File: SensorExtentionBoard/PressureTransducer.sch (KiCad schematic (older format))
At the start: 10 parts

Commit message: Added Hall Effect sensor test circuit
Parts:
- removed R? (x3): 768, symbol Device:R
- removed R? (x3): 12, symbol Device:R
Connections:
- wire segments 39 -> 18
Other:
- note removed: "Each pair of resistors in voltage divider must have a similar temperature coefficient (like from the same resistor family)"
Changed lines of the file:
@@
 	4900 3350 4900 3300
 NoConn ~ 5500 3100
-$Comp
-L Device:R R?
-U 1 1 5E062611
-P 5700 3300
-F 0 "R?" H 5770 3346 50  0000 L CNN
-F 1 "768" H 5770 3255 50  0000 L CNN
-F 2 "" V 5630 3300 50  0001 C CNN
-F 3 "~" H 5700 3300 50  0001 C CNN
-	1    5700 3300
-	1    0    0    -1
-$EndComp
-$Comp
-L Device:R R?
-U 1 1 5E062617
-P 5700 3900
-F 0 "R?" H 5770 3946 50  0000 L CNN
-F 1 "12" H 5770 3855 50  0000 L CNN
-F 2 "" V 5630 3900 50  0001 C CNN
-F 3 "~" H 5700 3900 50  0001 C CNN
-	1    5700 3900
-	1    0    0    -1
-$EndComp
-Wire Wire Line
-	6300 3450 6300 3500
-Wire Wire Line
-	6000 3450 6000 3600
-Wire Wire Line
-	5700 3450 5700 3700
-Wire Wire Line
-	6300 3500 6750 3500
-Connection ~ 6300 3500
-Wire Wire Line
-	6300 3500 6300 3750
-Wire Wire Line
-	6000 3600 6750 3600
-Connection ~ 6000 3600
-Wire Wire Line
-	6000 3600 6000 3750
-Wire Wire Line
-	5700 3700 6750 3700
-Connection ~ 5700 3700
-Wire Wire Line
-	5700 3700 5700 3750
-Wire Wire Line
-	5500 3000 5700 3000
-Wire Wire Line
-	5700 3000 5700 3150
-Wire Wire Line
-	5500 2900 6000 2900
-Wire Wire Line
-	6000 2900 6000 3150
-Wire Wire Line
-	5500 2800 6300 2800
-Wire Wire Line
-	6300 2800 6300 3150
-$Comp
-L power:GND #PWR?
-U 1 1 5E068856
-P 5700 4150
-F 0 "#PWR?" H 5700 3900 50  0001 C CNN
-F 1 "GND" H 5705 3977 50  0000 C CNN
-F 2 "" H 5700 4150 50  0001 C CNN
-F 3 "" H 5700 4150 50  0001 C CNN
-	1    5700 4150
-	1    0    0    -1
-$EndComp
-Wire Wire Line
-	5700 4050 5700 4100
-Wire Wire Line
-	5700 4100 6000 4100
-Wire Wire Line
-	6000 4100 6000 4050
-Connection ~ 5700 4100
-Wire Wire Line
-	5700 4100 5700 4150
-Wire Wire Line
-	6000 4100 6300 4100
-Wire Wire Line
-	6300 4100 6300 4050
-Connection ~ 6000 4100
-Text Label 6750 3500 0    50   ~ 0
+Text Label 5500 2800 0    50   ~ 0
 PT0
-Text Label 6750 3600 0    50   ~ 0
+Text Label 5500 2900 0    50   ~ 0
 PT1
-Text Label 6750 3700 0    50   ~ 0
+Text Label 5500 3000 0    50   ~ 0
 PT2
 Wire Wire Line
@@
 Wire Wire Line
 	4300 3100 4250 3100
-Text Notes 5700 2300 0    50   ~ 0
-Each pair of resistors in voltage divider must have a similar temperature coefficient (like from the same resistor family)
-$Comp
-L Device:R R?
-U 1 1 5EAFB0C7
-P 6000 3300
-F 0 "R?" H 6070 3346 50  0000 L CNN
-F 1 "768" H 6070 3255 50  0000 L CNN
-F 2 "" V 5930 3300 50  0001 C CNN
-F 3 "~" H 6000 3300 50  0001 C CNN
-	1    6000 3300
-	1    0    0    -1
-$EndComp
-$Comp
-L Device:R R?
-U 1 1 5EAFB244
-P 6300 3300
-F 0 "R?" H 6370 3346 50  0000 L CNN
-F 1 "768" H 6370 3255 50  0000 L CNN
-F 2 "" V 6230 3300 50  0001 C CNN
-F 3 "~" H 6300 3300 50  0001 C CNN
-	1    6300 3300
-	1    0    0    -1
-$EndComp
-$Comp
-L Device:R R?
-U 1 1 5EAFB46A
-P 6000 3900
-F 0 "R?" H 6070 3946 50  0000 L CNN
-F 1 "12" H 6070 3855 50  0000 L CNN
-F 2 "" V 5930 3900 50  0001 C CNN
-F 3 "~" H 6000 3900 50  0001 C CNN
-	1    6000 3900
-	1    0    0    -1
-$EndComp
-$Comp
-L Device:R R?
-U 1 1 5EAFB66D
-P 6300 3900
-F 0 "R?" H 6370 3946 50  0000 L CNN
-F 1 "12" H 6370 3855 50  0000 L CNN
-F 2 "" V 6230 3900 50  0001 C CNN
-F 3 "~" H 6300 3900 50  0001 C CNN
-	1    6300 3900
-	1    0    0    -1
-$EndComp
 $EndSCHEMATC

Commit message: Added top level page and made various fixes in other pages of SEB test rig board
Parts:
- added R101, R103, R105: 768, Resistor_SMD:R_1206_3216Metric_Pad1.42x1.75mm_HandSolder, symbol Device:R
- added R102, R104, R106: 100, Resistor_SMD:R_1206_3216Metric_Pad1.42x1.75mm_HandSolder, symbol Device:R
- added U9: ADS1115IDGS, Package_SO:TSSOP-10_3x3mm_P0.5mm, symbol Analog_ADC:ADS1115IDGS
- gave numbers to parts that had none: 4
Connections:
- net labels added: PT0_VIN, PT1_VIN, PT2_VIN, PT_ADC_ALERT_RDY, PT_ADC_SCL, PT_ADC_SDA, PT_DAC_RDY_~BSY, PT_DAC_SCL, PT_DAC_SDA, PT_DAC_~LDAC
- net labels removed: PT_RDY_~BSY, PT_SCL, PT_SDA, VCC, ~PT_LDAC
- wire segments 18 -> 40
- no-connect marks 1 -> 2

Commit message: Moved some stuff and added footprints to components
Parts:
- J12, J13, J14: footprint (none) -> Connector_Molex:Molex_MicroClasp_55932-0310_1x03_P2.00mm_Vertical
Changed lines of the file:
@@
 F 0 "J14" H 7722 4082 50  0000 R CNN
 F 1 "Conn_01x03_Male" H 7722 4173 50  0000 R CNN
-F 2 "" H 7750 4150 50  0001 C CNN
+F 2 "Connector_Molex:Molex_MicroClasp_55932-0310_1x03_P2.00mm_Vertical" H 7750 4150 50  0001 C CNN
 F 3 "~" H 7750 4150 50  0001 C CNN
 	1    7750 4150
@@
 F 0 "J13" H 7722 3532 50  0000 R CNN
 F 1 "Conn_01x03_Male" H 7722 3623 50  0000 R CNN
-F 2 "" H 7750 3600 50  0001 C CNN
+F 2 "Connector_Molex:Molex_MicroClasp_55932-0310_1x03_P2.00mm_Vertical" H 7750 3600 50  0001 C CNN
 F 3 "~" H 7750 3600 50  0001 C CNN
 	1    7750 3600
@@
 F 0 "J12" H 7722 2982 50  0000 R CNN
 F 1 "Conn_01x03_Male" H 7722 3073 50  0000 R CNN
-F 2 "" H 7750 3050 50  0001 C CNN
+F 2 "Connector_Molex:Molex_MicroClasp_55932-0310_1x03_P2.00mm_Vertical" H 7750 3050 50  0001 C CNN
 F 3 "~" H 7750 3050 50  0001 C CNN
 	1    7750 3050

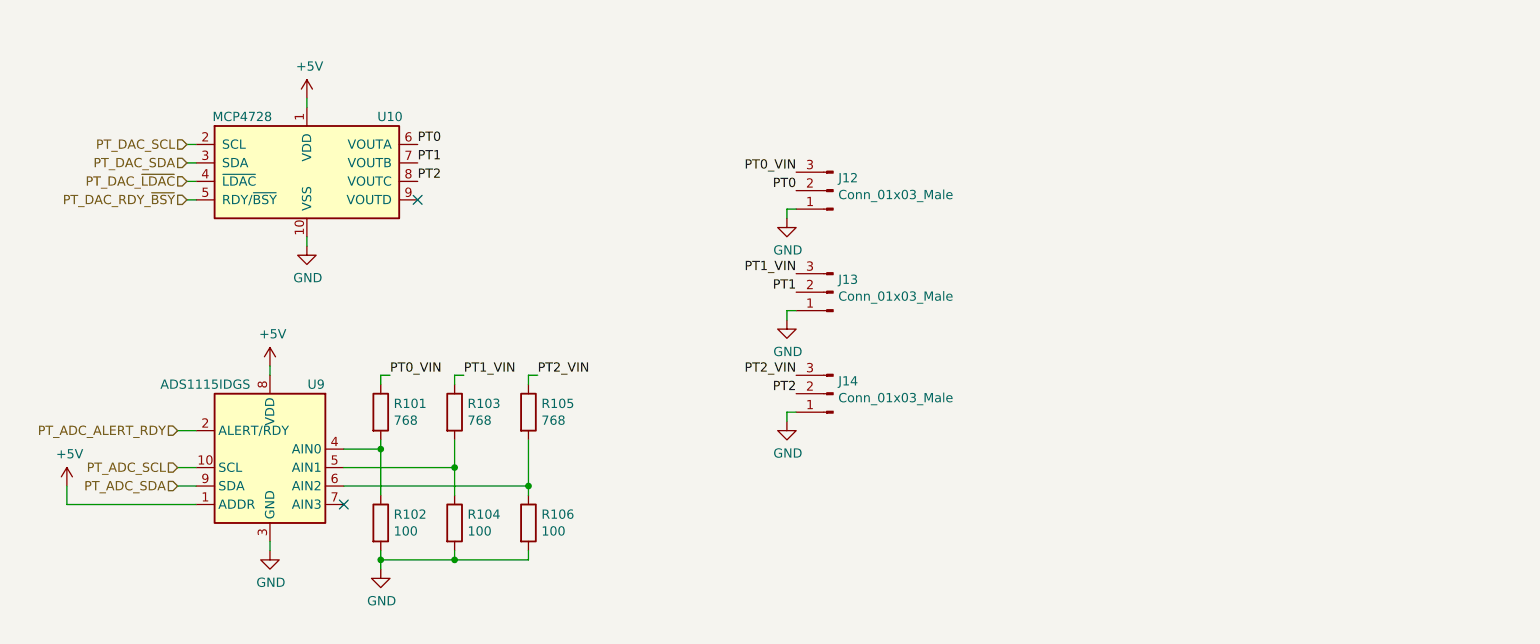
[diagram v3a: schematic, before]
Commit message: Added decoupling caps
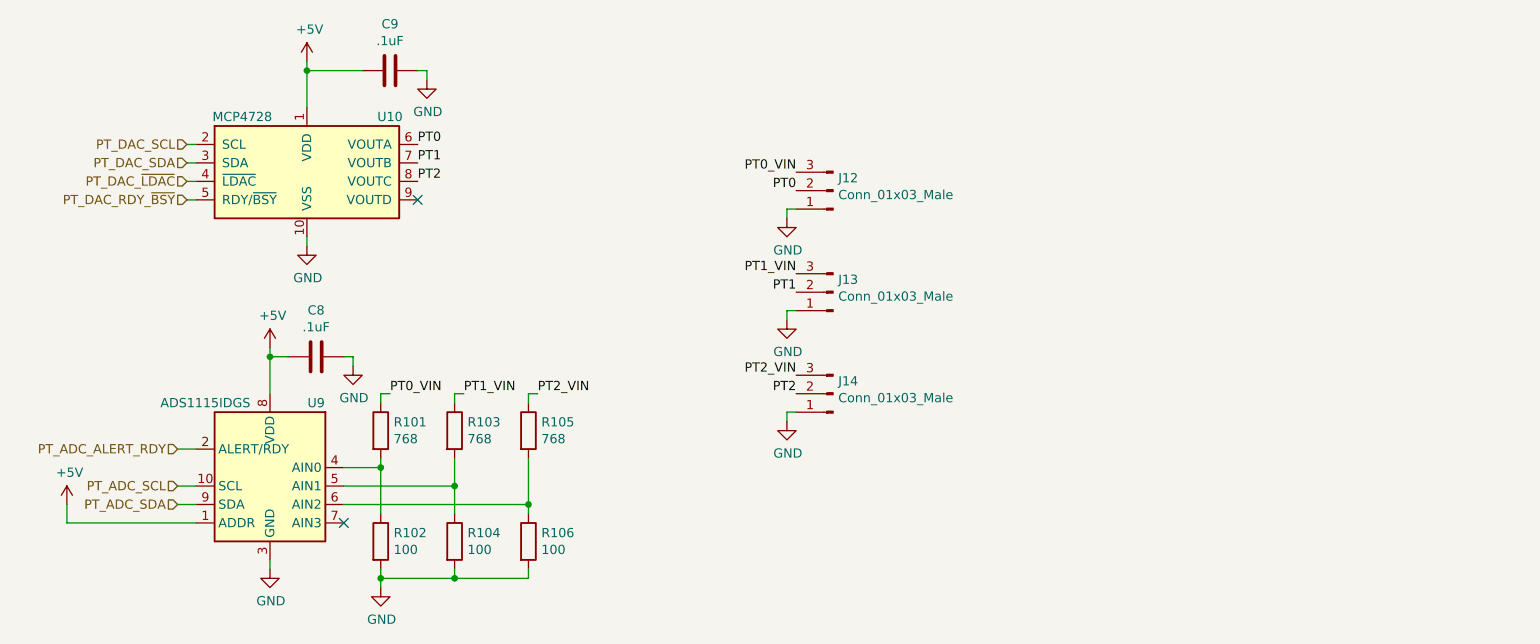
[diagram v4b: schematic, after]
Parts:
- added C8, C9: .1uF, symbol Device:C
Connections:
- net +5V: now also C8.2, C9.2
- net GND: now also C8.1, C9.1
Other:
- moved on the sheet: R101, R102, R103, R104, R105, R106, U9

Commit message: Replaced ADS1115 with ADS1015 on PT page
The ADS1115 is being used to read the voltages provided by the Helix
system to the pressure transducers. The ADS1015 is already doing
the same job for the Hall Effect sensors, however the ADS1015 has
4 bits lower accuracy. High accuracy is not needed for this
application so be replacing the ADS1115 with the ADS1015 we can
reduce cost and more importantly reduce BOM size making the project
logistics easier to manage.
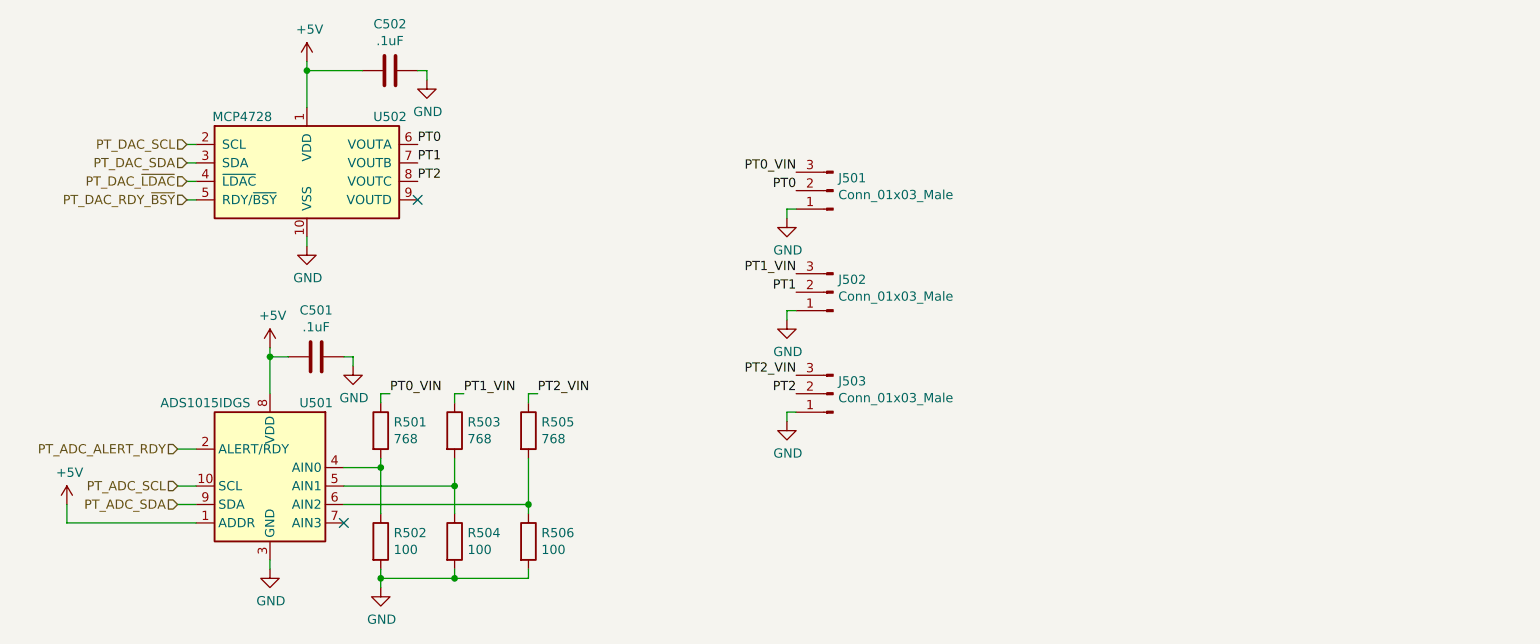
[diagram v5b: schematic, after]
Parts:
- removed U9: ADS1115IDGS, Package_SO:TSSOP-10_3x3mm_P0.5mm, symbol Analog_ADC:ADS1115IDGS
- added U501: ADS1015IDGS, Package_SO:TSSOP-10_3x3mm_P0.5mm, symbol Analog_ADC:ADS1015IDGS
- renumbered C8 to C501, C9 to C502, J12 to J501, J13 to J502, J14 to J503, R101 to R501, R102 to R502, R103 to R503, R104 to R504, R105 to R505, R106 to R506, U10 to U502
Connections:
- net +5V: now also U501.1 (ADDR), U501.8 (VDD)
- net GND: now also U501.3 (GND)
- net PT_ADC_ALERT_RDY: now also U501.2 (ALERT/RDY)
- net PT_ADC_SCL: now also U501.10 (SCL)
- net PT_ADC_SDA: now also U501.9 (SDA)
- net at R501.2, R502.1: now also U501.4 (AIN0)
- net at R503.2, R504.1: now also U501.5 (AIN1)
- net at R505.2, R506.1: now also U501.6 (AIN2)
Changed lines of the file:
@@
 $EndDescr
 $Comp
-L Analog_DAC:MCP4728 U10
+L Analog_DAC:MCP4728 U502
 U 1 1 5E05A1D5
 P 4900 2900
-F 0 "U10" H 5350 3150 50  0000 C CNN
+F 0 "U502" H 5350 3150 50  0000 C CNN
 F 1 "MCP4728" H 4550 3150 50  0000 C CNN
 F 2 "Package_SO:MSOP-10_3x3mm_P0.5mm" H 4900 2300 50  0001 C CNN
@@
 $EndComp
 $Comp
-L power:+5V #PWR047
+L power:+5V #PWR0504
 U 1 1 5E05A95B
 P 4900 2350
-F 0 "#PWR047" H 4900 2200 50  0001 C CNN
+F 0 "#PWR0504" H 4900 2200 50  0001 C CNN
 F 1 "+5V" H 4915 2523 50  0000 C CNN
 F 2 "" H 4900 2350 50  0001 C CNN
@@
 	4900 2600 4900 2400
 $Comp
-L power:GND #PWR048
+L power:GND #PWR0505
 U 1 1 5E05AE1F
 P 4900 3350
-F 0 "#PWR048" H 4900 3100 50  0001 C CNN
+F 0 "#PWR0505" H 4900 3100 50  0001 C CNN
 F 1 "GND" H 4905 3177 50  0000 C CNN
 F 2 "" H 4900 3350 50  0001 C CNN
@@
 	7500 3200 7500 3150
 $Comp
-L power:GND #PWR052
+L power:GND #PWR0509
 U 1 1 5E071F60
 P 7500 3200
-F 0 "#PWR052" H 7500 2950 50  0001 C CNN
+F 0 "#PWR0509" H 7500 2950 50  0001 C CNN
 F 1 "GND" H 7505 3027 50  0000 C CNN
 F 2 "" H 7500 3200 50  0001 C CNN
@@
 	7500 3750 7500 3700
 $Comp
-L power:GND #PWR053
+L power:GND #PWR0510
 U 1 1 5E06CCB7
 P 7500 3750
-F 0 "#PWR053" H 7500 3500 50  0001 C CNN
+F 0 "#PWR0510" H 7500 3500 50  0001 C CNN
 F 1 "GND" H 7505 3577 50  0000 C CNN
 F 2 "" H 7500 3750 50  0001 C CNN
@@
 	7500 4300 7500 4250
 $Comp
-L power:GND #PWR054
+L power:GND #PWR0511
 U 1 1 5E06C38E
 P 7500 4300
-F 0 "#PWR054" H 7500 4050 50  0001 C CNN
+F 0 "#PWR0511" H 7500 4050 50  0001 C CNN
 F 1 "GND" H 7505 4127 50  0000 C CNN
 F 2 "" H 7500 4300 50  0001 C CNN
@@
 PT0
 $Comp
-L Connector:Conn_01x03_Male J14
+L Connector:Conn_01x03_Male J503
 U 1 1 5E06B5DF
 P 7750 4150
-F 0 "J14" H 7722 4082 50  0000 R CNN
+F 0 "J503" H 7722 4082 50  0000 R CNN
 F 1 "Conn_01x03_Male" H 7722 4173 50  0000 R CNN
 F 2 "Connector_Molex:Molex_MicroClasp_55932-0310_1x03_P2.00mm_Vertical" H 7750 4150 50  0001 C CNN
@@
 $EndComp
 $Comp
-L Connector:Conn_01x03_Male J13
+L Connector:Conn_01x03_Male J502
 U 1 1 5E06B2C3
 P 7750 3600
-F 0 "J13" H 7722 3532 50  0000 R CNN
+F 0 "J502" H 7722 3532 50  0000 R CNN
 F 1 "Conn_01x03_Male" H 7722 3623 50  0000 R CNN
 F 2 "Connector_Molex:Molex_MicroClasp_55932-0310_1x03_P2.00mm_Vertical" H 7750 3600 50  0001 C CNN
@@
 $EndComp
 $Comp
-L Connector:Conn_01x03_Male J12
+L Connector:Conn_01x03_Male J501
 U 1 1 5E069F3E
 P 7750 3050
-F 0 "J12" H 7722 2982 50  0000 R CNN
+F 0 "J501" H 7722 2982 50  0000 R CNN
 F 1 "Conn_01x03_Male" H 7722 3073 50  0000 R CNN
 F 2 "Connector_Molex:Molex_MicroClasp_55932-0310_1x03_P2.00mm_Vertical" H 7750 3050 50  0001 C CNN
@@
 PT2_VIN
 $Comp
-L Analog_ADC:ADS1115IDGS U9
-U 1 1 5E3D1890
-P 4700 4650
-F 0 "U9" H 4450 5100 50  0000 C CNN
-F 1 "ADS1115IDGS" H 5050 5100 50  0000 C CNN
-F 2 "Package_SO:TSSOP-10_3x3mm_P0.5mm" H 4700 4150 50  0001 C CNN
-F 3 "http://www.ti.com/lit/ds/symlink/ads1113.pdf" H 4650 3750 50  0001 C CNN
-	1    4700 4650
-	-1   0    0    -1
-$EndComp
-$Comp
-L Device:R R105
+L Device:R R505
 U 1 1 5E3D7CC3
 P 6100 4350
-F 0 "R105" H 6170 4396 50  0000 L CNN
+F 0 "R505" H 6170 4396 50  0000 L CNN
 F 1 "768" H 6170 4305 50  0000 L CNN
 F 2 "Resistor_SMD:R_1206_3216Metric_Pad1.42x1.75mm_HandSolder" V 6030 4350 50  0001 C CNN
@@
 Connection ~ 5300 4550
 $Comp
-L power:GND #PWR046
+L power:GND #PWR0503
 U 1 1 5E3D9ED4
 P 4700 5100
-F 0 "#PWR046" H 4700 4850 50  0001 C CNN
+F 0 "#PWR0503" H 4700 4850 50  0001 C CNN
 F 1 "GND" H 4705 4927 50  0000 C CNN
 F 2 "" H 4700 5100 50  0001 C CNN
@@
 $EndComp
 $Comp
-L power:GND #PWR050
+L power:GND #PWR0507
 U 1 1 5E3DACE8
 P 5300 5200
-F 0 "#PWR050" H 5300 4950 50  0001 C CNN
+F 0 "#PWR0507" H 5300 4950 50  0001 C CNN
 F 1 "GND" H 5305 5027 50  0000 C CNN
 F 2 "" H 5300 5200 50  0001 C CNN
@@
 	6100 4150 6100 4200
 $Comp
-L power:+5V #PWR045
+L power:+5V #PWR0502
 U 1 1 5E3E1CCE
 P 4700 3900
-F 0 "#PWR045" H 4700 3750 50  0001 C CNN
+F 0 "#PWR0502" H 4700 3750 50  0001 C CNN
 F 1 "+5V" H 4715 4073 50  0000 C CNN
 F 2 "" H 4700 3900 50  0001 C CNN
@@
 	4200 4450 4300 4450
 $Comp
-L power:+5V #PWR044
+L power:+5V #PWR0501
 U 1 1 5E3E9881
 P 3600 4750
-F 0 "#PWR044" H 3600 4600 50  0001 C CNN
+F 0 "#PWR0501" H 3600 4600 50  0001 C CNN
 F 1 "+5V" H 3615 4923 50  0000 C CNN
 F 2 "" H 3600 4750 50  0001 C CNN
@@
 P 5300 4950
 AR Path="/5E630276" Ref="R?"  Part="1"
-AR Path="/5E059EAC/5E630276" Ref="R102"  Part="1"
-F 0 "R102" H 5370 4996 50  0000 L CNN
+AR Path="/5E059EAC/5E630276" Ref="R502"  Part="1"
+F 0 "R502" H 5370 4996 50  0000 L CNN
 F 1 "100" H 5370 4905 50  0000 L CNN
 F 2 "Resistor_SMD:R_1206_3216Metric_Pad1.42x1.75mm_HandSolder" V 5230 4950 50  0001 C CNN
@@
 P 5700 4950
 AR Path="/5E63145E" Ref="R?"  Part="1"
-AR Path="/5E059EAC/5E63145E" Ref="R104"  Part="1"
-F 0 "R104" H 5770 4996 50  0000 L CNN
+AR Path="/5E059EAC/5E63145E" Ref="R504"  Part="1"
+F 0 "R504" H 5770 4996 50  0000 L CNN
 F 1 "100" H 5770 4905 50  0000 L CNN
 F 2 "Resistor_SMD:R_1206_3216Metric_Pad1.42x1.75mm_HandSolder" V 5630 4950 50  0001 C CNN
@@
 P 6100 4950
 AR Path="/5E631AFF" Ref="R?"  Part="1"
-AR Path="/5E059EAC/5E631AFF" Ref="R106"  Part="1"
-F 0 "R106" H 6170 4996 50  0000 L CNN
+AR Path="/5E059EAC/5E631AFF" Ref="R506"  Part="1"
+F 0 "R506" H 6170 4996 50  0000 L CNN
 F 1 "100" H 6170 4905 50  0000 L CNN
 F 2 "Resistor_SMD:R_1206_3216Metric_Pad1.42x1.75mm_HandSolder" V 6030 4950 50  0001 C CNN
@@
 $EndComp
 $Comp
-L Device:R R103
+L Device:R R503
 U 1 1 5E639E33
 P 5700 4350
-F 0 "R103" H 5770 4396 50  0000 L CNN
+F 0 "R503" H 5770 4396 50  0000 L CNN
 F 1 "768" H 5770 4305 50  0000 L CNN
 F 2 "Resistor_SMD:R_1206_3216Metric_Pad1.42x1.75mm_HandSolder" V 5630 4350 50  0001 C CNN
@@
 $EndComp
 $Comp
-L Device:R R101
+L Device:R R501
 U 1 1 5E639FAD
 P 5300 4350
-F 0 "R101" H 5370 4396 50  0000 L CNN
+F 0 "R501" H 5370 4396 50  0000 L CNN
 F 1 "768" H 5370 4305 50  0000 L CNN
 F 2 "Resistor_SMD:R_1206_3216Metric_Pad1.42x1.75mm_HandSolder" V 5230 4350 50  0001 C CNN
@@
 P 5350 2400
 AR Path="/5E13E0B3" Ref="C?"  Part="1"
-AR Path="/5E059EAC/5E13E0B3" Ref="C9"  Part="1"
-F 0 "C9" V 5098 2400 50  0000 C CNN
+AR Path="/5E059EAC/5E13E0B3" Ref="C502"  Part="1"
+F 0 "C502" V 5098 2400 50  0000 C CNN
 F 1 ".1uF" V 5189 2400 50  0000 C CNN
 F 2 "" H 5388 2250 50  0001 C CNN
@@
 P 5550 2450
 AR Path="/5E13E0B9" Ref="#PWR?"  Part="1"
-AR Path="/5E059EAC/5E13E0B9" Ref="#PWR051"  Part="1"
-F 0 "#PWR051" H 5550 2200 50  0001 C CNN
+AR Path="/5E059EAC/5E13E0B9" Ref="#PWR0508"  Part="1"
+F 0 "#PWR0508" H 5550 2200 50  0001 C CNN
 F 1 "GND" H 5555 2277 50  0000 C CNN
 F 2 "" H 5550 2450 50  0001 C CNN
@@
 P 4950 3950
 AR Path="/5E1425A7" Ref="C?"  Part="1"
-AR Path="/5E059EAC/5E1425A7" Ref="C8"  Part="1"
-F 0 "C8" V 4698 3950 50  0000 C CNN
+AR Path="/5E059EAC/5E1425A7" Ref="C501"  Part="1"
+F 0 "C501" V 4698 3950 50  0000 C CNN
 F 1 ".1uF" V 4789 3950 50  0000 C CNN
 F 2 "" H 4988 3800 50  0001 C CNN
@@
 P 5150 4000
 AR Path="/5E1425AD" Ref="#PWR?"  Part="1"
-AR Path="/5E059EAC/5E1425AD" Ref="#PWR049"  Part="1"
-F 0 "#PWR049" H 5150 3750 50  0001 C CNN
+AR Path="/5E059EAC/5E1425AD" Ref="#PWR0506"  Part="1"
+F 0 "#PWR0506" H 5150 3750 50  0001 C CNN
 F 1 "GND" H 5155 3827 50  0000 C CNN
 F 2 "" H 5150 4000 50  0001 C CNN
@@
 Wire Wire Line
 	4700 3950 4700 4150
+$Comp
+L Analog_ADC:ADS1015IDGS U501
+U 1 1 5E1F9CD6
+P 4700 4650
+F 0 "U501" H 4450 5100 50  0000 C CNN
+F 1 "ADS1015IDGS" H 5050 5100 50  0000 C CNN
+F 2 "Package_SO:TSSOP-10_3x3mm_P0.5mm" H 4700 4150 50  0001 C CNN
+F 3 "http://www.ti.com/lit/ds/symlink/ads1015.pdf" H 4650 3750 50  0001 C CNN
+	1    4700 4650
+	-1   0    0    -1
+$EndComp
 $EndSCHEMATC
